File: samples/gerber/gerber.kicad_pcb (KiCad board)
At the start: 2 copper layers, 50 x 50 mm, 7 parts, among them J1 USB_C_Receptacle_USB2.0_16P, J2 Conn_01x04_Socket, U1 W25Q16JVSS

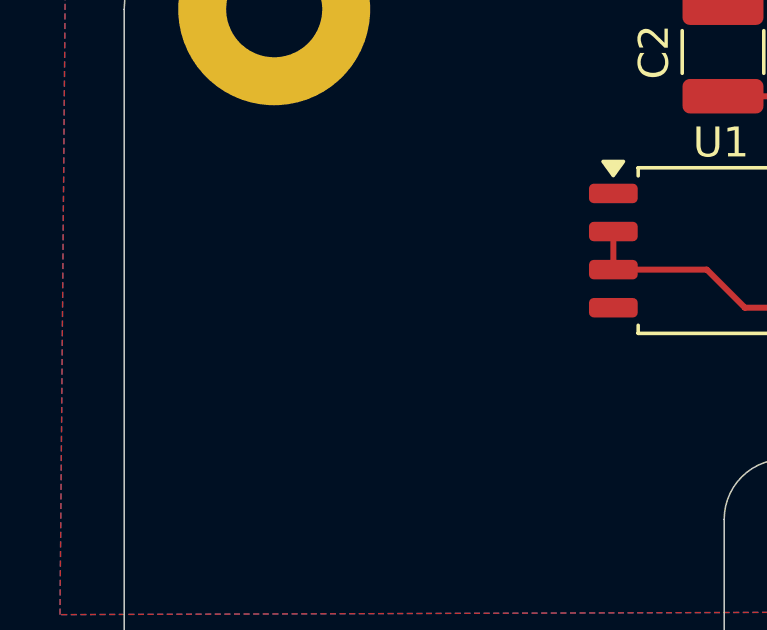
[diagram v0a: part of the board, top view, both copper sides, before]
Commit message: sample/gerber: add rotated footprint
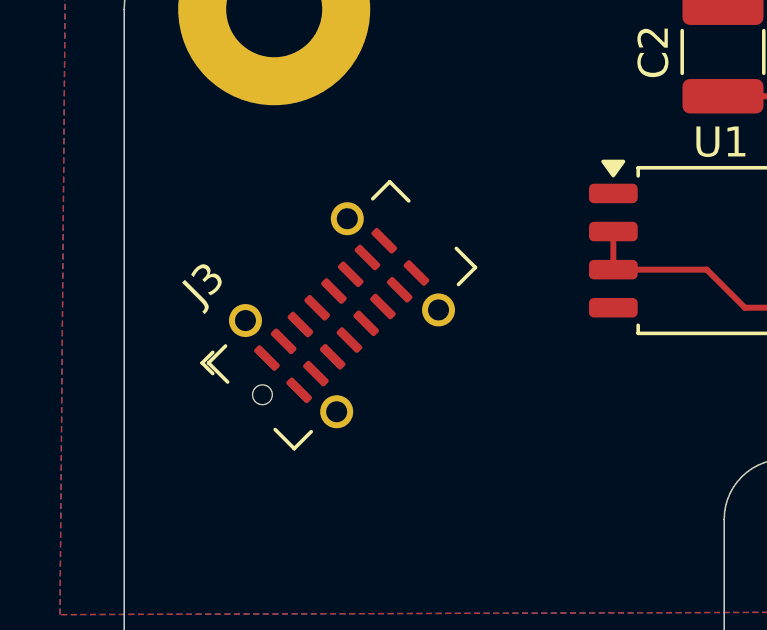
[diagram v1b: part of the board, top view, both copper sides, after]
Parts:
- added J3: USB_C_Receptacle_USB2.0_16P, Connector_USB:USB_C_Receptacle_G-Switch_GT-USB-7051x, F.Cu at (107.3, 115.2)
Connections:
- J1 pad A1: unconnected-(J1-GND-PadA1)_3 -> GND
- J1 pad A12: unconnected-(J1-GND-PadA1)_1 -> GND
- J1 pad B1: unconnected-(J1-GND-PadA1)_2 -> GND
- J1 pad B12: unconnected-(J1-GND-PadA1) -> GND
- J1 pad S1: unconnected-(J1-SHIELD-PadS1) -> GND

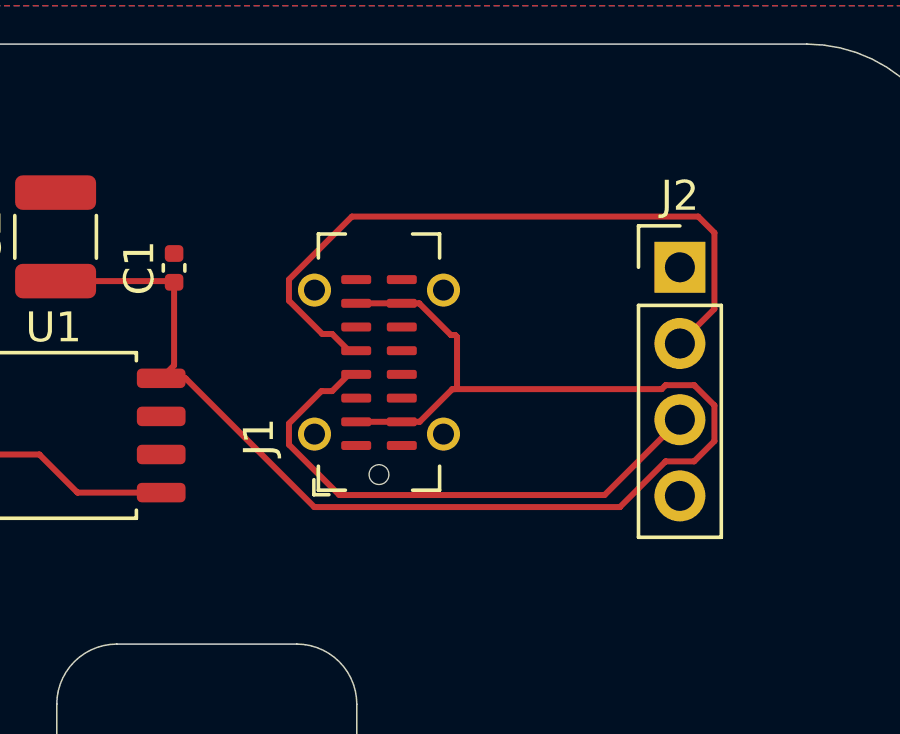
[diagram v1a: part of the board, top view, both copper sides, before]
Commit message: update sample gerber: add arc
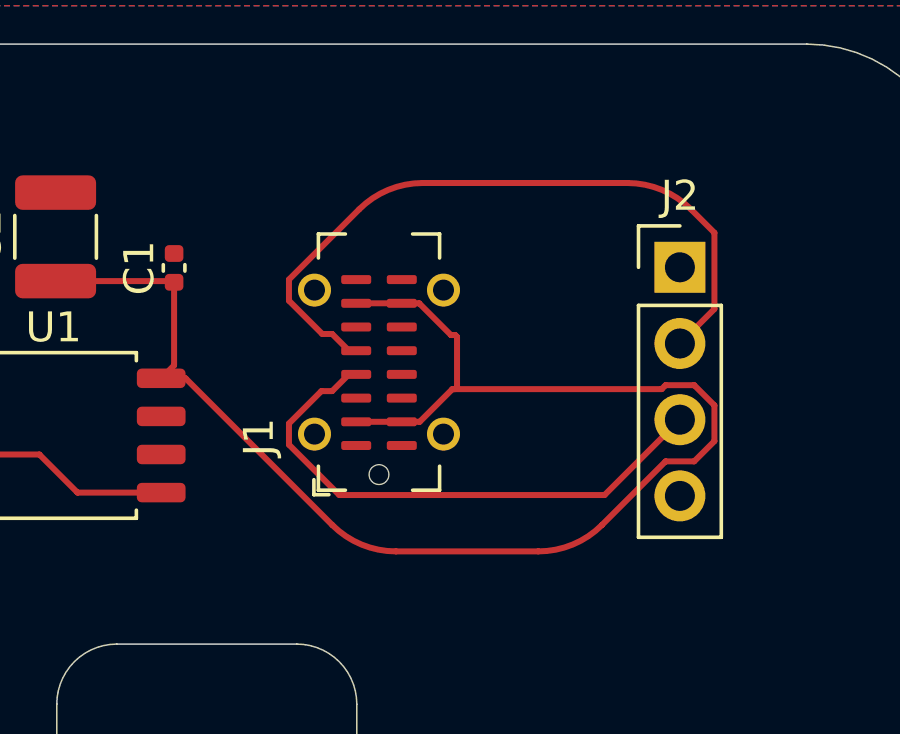
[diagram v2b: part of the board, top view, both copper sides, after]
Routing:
- net /V: track 47.7 -> 48.6 mm
- net Net-(J2-Pin_2): track 23.1 -> 23.7 mm
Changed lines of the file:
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@@
 	)
 	(segment
-		(start 129.837504 105.749)
+		(start 129.179 109.662824)
+		(end 129.736176 110.22)
+		(width 0.2)
+		(layer "F.Cu")
+		(net 10)
+	)
+	(segment
+		(start 140.77 109.98)
+		(end 141.921 108.829)
+		(width 0.2)
+		(layer "F.Cu")
+		(net 10)
+	)
+	(segment
+		(start 130.077824 105.50868)
 		(end 127.739 107.847504)
 		(width 0.2)
@@
 	)
 	(segment
-		(start 141.381 105.749)
-		(end 129.837504 105.749)
+		(start 139.019359 104.63)
+		(end 132.199145 104.63)
+		(width 0.2)
+		(layer "F.Cu")
+		(net 10)
+	)
+	(segment
+		(start 141.921 106.289)
+		(end 141.140679 105.508679)
+		(width 0.2)
+		(layer "F.Cu")
+		(net 10)
+	)
+	(segment
+		(start 127.739 107.847504)
+		(end 127.739 108.552496)
+		(width 0.2)
+		(layer "F.Cu")
+		(net 10)
+	)
+	(segment
+		(start 128.849328 109.662824)
+		(end 129.179 109.662824)
 		(width 0.2)
 		(layer "F.Cu")
@@
 	)
 	(segment
-		(start 128.849328 109.662824)
-		(end 129.179 109.662824)
-		(width 0.2)
-		(layer "F.Cu")
-		(net 10)
-	)
-	(segment
-		(start 140.77 109.98)
-		(end 141.921 108.829)
-		(width 0.2)
-		(layer "F.Cu")
-		(net 10)
-	)
-	(segment
-		(start 141.921 106.289)
-		(end 141.381 105.749)
+		(start 141.921 108.829)
+		(end 141.921 106.289)
 		(width 0.2)
 		(layer "F.Cu")
@@
 		(net 10)
 	)
-	(segment
-		(start 129.179 109.662824)
-		(end 129.736176 110.22)
-		(width 0.2)
-		(layer "F.Cu")
-		(net 10)
-	)
-	(segment
-		(start 127.739 107.847504)
-		(end 127.739 108.552496)
-		(width 0.2)
-		(layer "F.Cu")
-		(net 10)
-	)
-	(segment
-		(start 141.921 108.829)
-		(end 141.921 106.289)
+	(arc
+		(start 130.077824 105.50868)
+		(mid 131.051094 104.858361)
+		(end 132.199145 104.63)
+		(width 0.2)
+		(layer "F.Cu")
+		(net 10)
+	)
+	(arc
+		(start 139.019359 104.63)
+		(mid 140.167409 104.858361)
+		(end 141.140679 105.508679)
 		(width 0.2)
 		(layer "F.Cu")
@@
 	)
 	(segment
+		(start 141.24676 111.369)
+		(end 141.921 112.04324)
+		(width 0.2)
+		(layer "F.Cu")
+		(net 22)
+	)
+	(segment
 		(start 133.341 109.758164)
 		(end 133.341 111.441836)
@@
 	)
 	(segment
+		(start 133.185504 111.501)
+		(end 140.16124 111.501)
+		(width 0.2)
+		(layer "F.Cu")
+		(net 22)
+	)
+	(segment
 		(start 132.08 108.64)
 		(end 133.139 109.699)
@@
 	)
 	(segment
+		(start 141.24676 113.909)
+		(end 140.29324 113.909)
+		(width 0.2)
+		(layer "F.Cu")
+		(net 22)
+	)
+	(segment
+		(start 136.049599 116.91)
+		(end 131.30514 116.91)
+		(width 0.2)
+		(layer "F.Cu")
+		(net 22)
+	)
+	(segment
+		(start 123.82 107.94)
+		(end 123.91 107.94)
+		(width 0.2)
+		(layer "F.Cu")
+		(net 22)
+	)
+	(segment
+		(start 123.78 107.9)
+		(end 123.82 107.94)
+		(width 0.2)
+		(layer "F.Cu")
+		(net 22)
+	)
+	(segment
+		(start 131.5 112.59)
+		(end 129.98 112.59)
+		(width 0.2)
+		(layer "F.Cu")
+		(net 22)
+	)
+	(segment
+		(start 133.281836 109.699)
+		(end 133.341 109.758164)
+		(width 0.2)
+		(layer "F.Cu")
+		(net 22)
+	)
+	(segment
+		(start 131.5 112.59)
+		(end 132.096504 112.59)
+		(width 0.2)
+		(layer "F.Cu")
+		(net 22)
+	)
+	(segment
+		(start 133.139 109.699)
+		(end 133.281836 109.699)
+		(width 0.2)
+		(layer "F.Cu")
+		(net 22)
+	)
+	(segment
+		(start 140.29324 113.909)
+		(end 138.170919 116.031321)
+		(width 0.2)
+		(layer "F.Cu")
+		(net 22)
+	)
+	(segment
+		(start 123.48 111.14)
+		(end 123.91 110.71)
+		(width 0.2)
+		(layer "F.Cu")
+		(net 22)
+	)
+	(segment
+		(start 129.183819 116.03132)
+		(end 124.292499 111.14)
+		(width 0.2)
+		(layer "F.Cu")
+		(net 22)
+	)
+	(segment
+		(start 133.281836 111.501)
+		(end 133.185504 111.501)
+		(width 0.2)
+		(layer "F.Cu")
+		(net 22)
+	)
+	(segment
+		(start 141.921 113.23476)
+		(end 141.24676 113.909)
+		(width 0.2)
+		(layer "F.Cu")
+		(net 22)
+	)
+	(segment
+		(start 141.921 112.04324)
+		(end 141.921 113.23476)
+		(width 0.2)
+		(layer "F.Cu")
+		(net 22)
+	)
+	(segment
 		(start 140.16124 111.501)
 		(end 140.29324 111.369)
@@
 	)
 	(segment
-		(start 128.584499 115.432)
-		(end 124.292499 111.14)
-		(width 0.2)
-		(layer "F.Cu")
-		(net 22)
-	)
-	(segment
-		(start 141.921 112.04324)
-		(end 141.921 113.23476)
-		(width 0.2)
-		(layer "F.Cu")
-		(net 22)
-	)
-	(segment
-		(start 123.82 107.94)
-		(end 123.91 107.94)
-		(width 0.2)
-		(layer "F.Cu")
-		(net 22)
-	)
-	(segment
-		(start 138.77024 115.432)
-		(end 128.584499 115.432)
-		(width 0.2)
-		(layer "F.Cu")
-		(net 22)
-	)
-	(segment
-		(start 123.78 107.9)
-		(end 123.82 107.94)
+		(start 133.341 111.441836)
+		(end 133.281836 111.501)
+		(width 0.2)
+		(layer "F.Cu")
+		(net 22)
+	)
+	(segment
+		(start 131.5 108.64)
+		(end 132.08 108.64)
 		(width 0.2)
 		(layer "F.Cu")
@@
 	)
 	(segment
-		(start 131.5 112.59)
-		(end 129.98 112.59)
-		(width 0.2)
-		(layer "F.Cu")
-		(net 22)
-	)
-	(segment
-		(start 141.24676 113.909)
-		(end 140.29324 113.909)
-		(width 0.2)
-		(layer "F.Cu")
-		(net 22)
-	)
-	(segment
-		(start 133.281836 109.699)
-		(end 133.341 109.758164)
-		(width 0.2)
-		(layer "F.Cu")
-		(net 22)
-	)
-	(segment
-		(start 131.5 112.59)
-		(end 132.096504 112.59)
-		(width 0.2)
-		(layer "F.Cu")
-		(net 22)
-	)
-	(segment
-		(start 133.139 109.699)
-		(end 133.281836 109.699)
-		(width 0.2)
-		(layer "F.Cu")
-		(net 22)
-	)
-	(segment
-		(start 133.185504 111.501)
-		(end 140.16124 111.501)
-		(width 0.2)
-		(layer "F.Cu")
-		(net 22)
-	)
-	(segment
-		(start 123.48 111.14)
-		(end 123.91 110.71)
-		(width 0.2)
-		(layer "F.Cu")
-		(net 22)
-	)
-	(segment
-		(start 133.281836 111.501)
-		(end 133.185504 111.501)
-		(width 0.2)
-		(layer "F.Cu")
-		(net 22)
-	)
-	(segment
-		(start 141.24676 111.369)
-		(end 141.921 112.04324)
-		(width 0.2)
-		(layer "F.Cu")
-		(net 22)
-	)
-	(segment
-		(start 133.341 111.441836)
-		(end 133.281836 111.501)
-		(width 0.2)
-		(layer "F.Cu")
-		(net 22)
-	)
-	(segment
-		(start 140.29324 113.909)
-		(end 138.77024 115.432)
-		(width 0.2)
-		(layer "F.Cu")
-		(net 22)
-	)
-	(segment
-		(start 131.5 108.64)
-		(end 132.08 108.64)
-		(width 0.2)
-		(layer "F.Cu")
-		(net 22)
-	)
-	(segment
 		(start 132.096504 112.59)
 		(end 133.185504 111.501)
@@
 	)
 	(segment
-		(start 141.921 113.23476)
-		(end 141.24676 113.909)
-		(width 0.2)
-		(layer "F.Cu")
-		(net 22)
-	)
-	(segment
 		(start 124.292499 111.14)
 		(end 123.48 111.14)
@@
 		(width 0.2)
 		(layer "F.Cu")
+		(net 22)
+	)
+	(arc
+		(start 129.183819 116.03132)
+		(mid 130.157089 116.681639)
+		(end 131.30514 116.91)
+		(width 0.2)
+		(layer "F.Cu")
+		(net 22)
+	)
+	(arc
+		(start 138.170919 116.031321)
+		(mid 137.197649 116.681639)
+		(end 136.049599 116.91)
+		(width 0.2)
+		(layer "F.Cu")

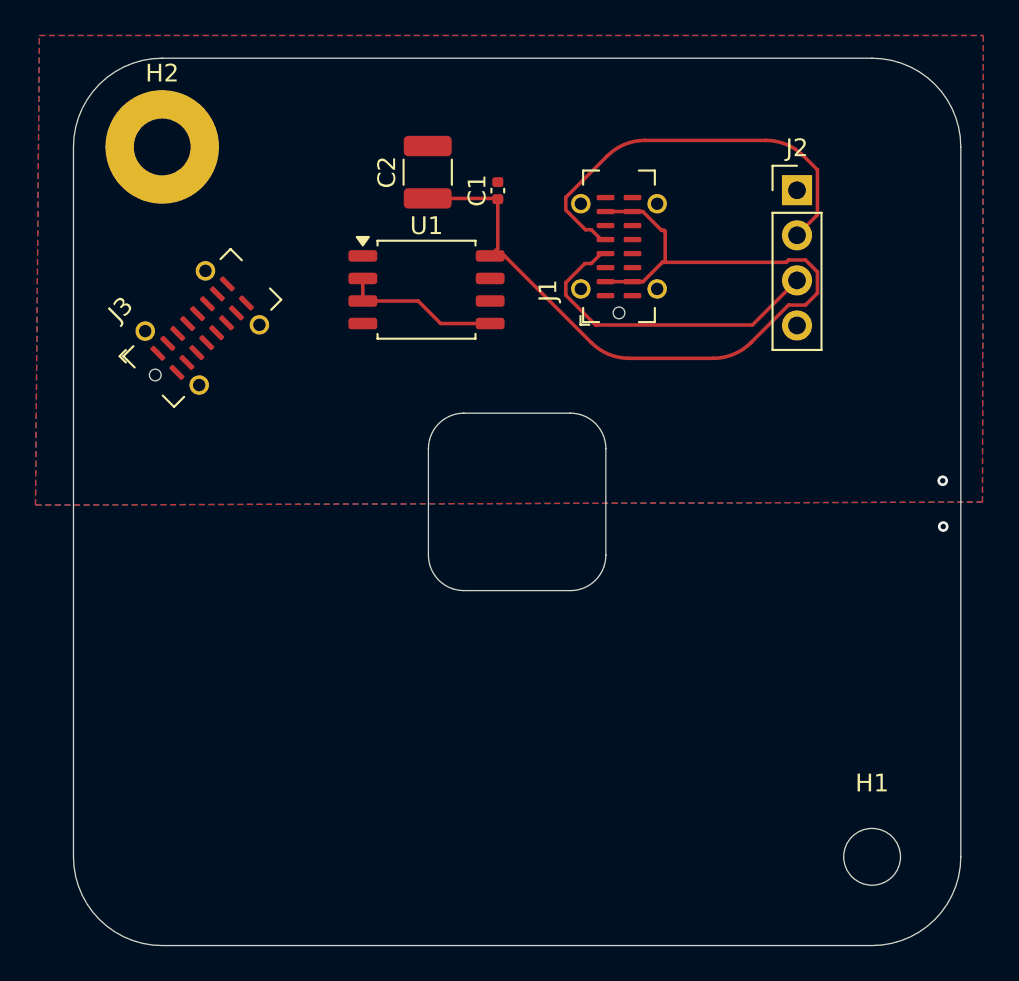
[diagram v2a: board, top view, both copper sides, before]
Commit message: gerber: handle kicad exported filenames
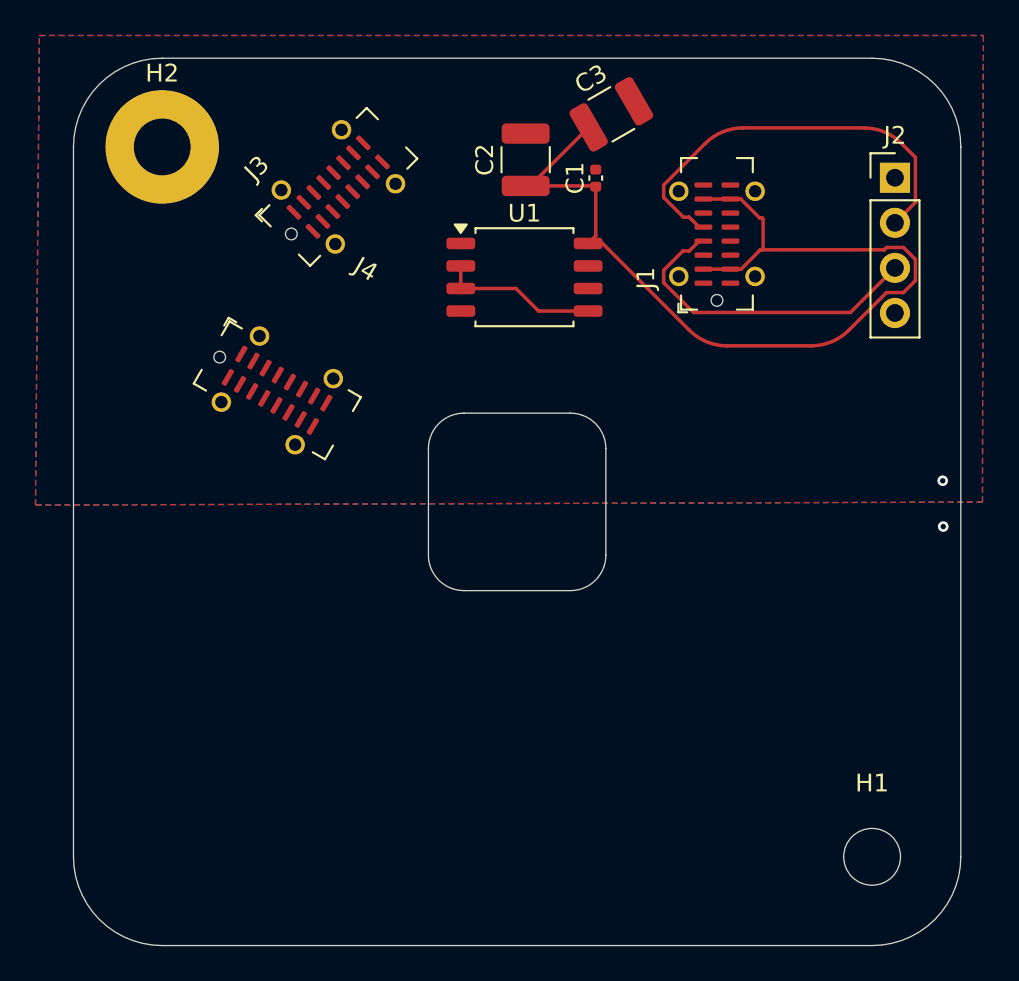
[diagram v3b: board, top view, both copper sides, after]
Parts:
- added C3: C, Capacitor_SMD:C_1210_3225Metric, F.Cu at (130.3, 103.2)
- added J4: USB_C_Receptacle_USB2.0_16P, Connector_USB:USB_C_Receptacle_G-Switch_GT-USB-7051x, F.Cu at (111.5, 118.7)
- moved J3 11.0 mm to (114.9, 107.3)
- moved C1 5.56 mm to (129.4, 106.8)
- moved C2 5.56 mm to (125.5, 105.7)
- moved J1 5.56 mm to (136.3, 109.9)
- moved J2 5.56 mm to (146.3, 106.7)
- moved U1 5.56 mm to (125.4, 112.3)
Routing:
- net /V: track 48.6 -> 53.5 mm
